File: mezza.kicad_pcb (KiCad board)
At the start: 2 copper layers, 85 x 54 mm, 6 parts, among them P1 CONN_02X20, P2 CONN_02X20

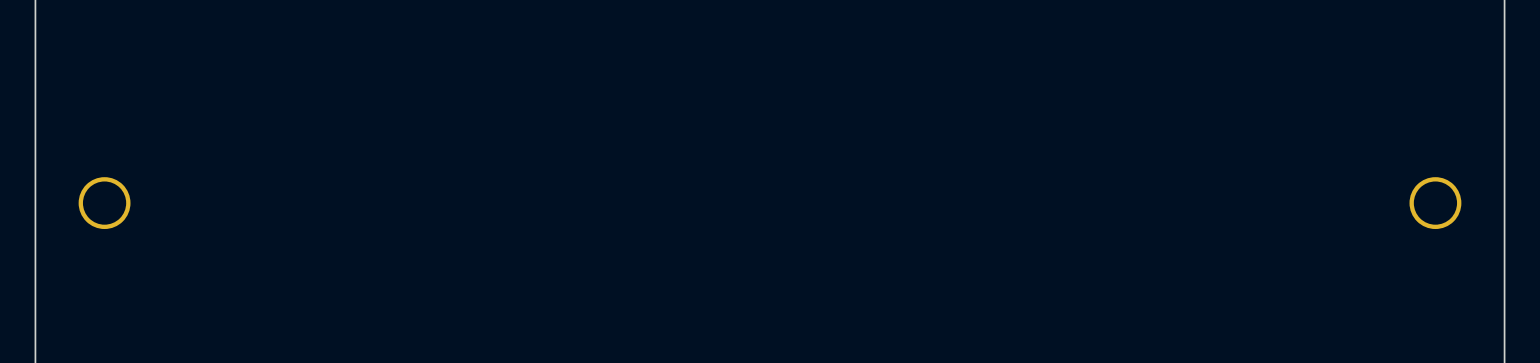
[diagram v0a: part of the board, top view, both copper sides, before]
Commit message: Add dimension markings to layout and correct hole positions
Add dimension markings to the template so that users can see exactly how
things are placed and compare them with the 96Boards spec. At the same
time, fix the position of 2 of the mounting holes and lock all the
footprints so they don't get accidentally changed.

Signed-off-by: Grant Likely <grant.likely@linaro.org>
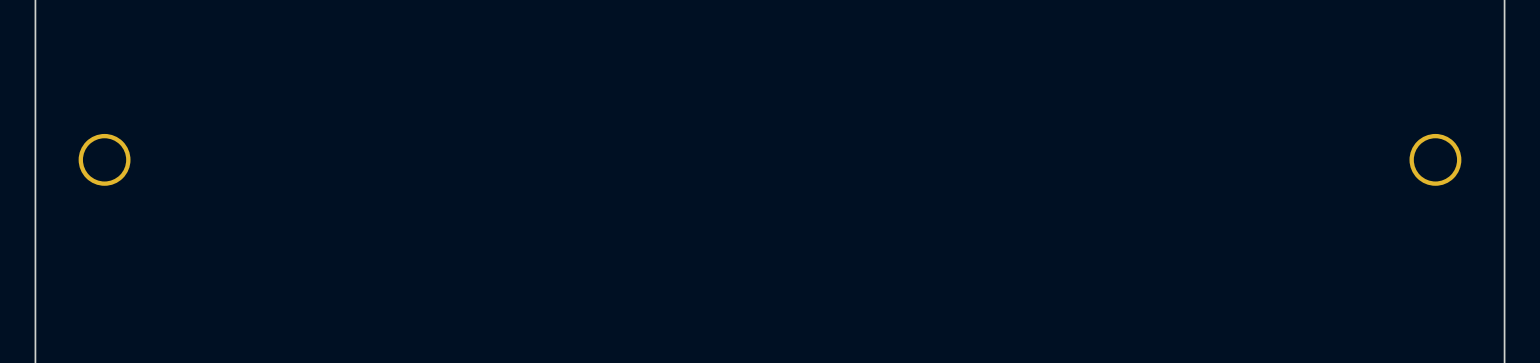
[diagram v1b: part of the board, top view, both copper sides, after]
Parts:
- moved REF** 2.50 mm to (104.0, 135.5)
- moved REF** 2.50 mm to (181.0, 135.5)
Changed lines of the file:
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@@
     (links 44)
     (no_connects 44)
-    (area 99.949999 99.949999 185.049493 154.050001)
+    (area 85.071429 87.15 185.633753 154.050001)
     (thickness 1.6)
-    (drawings 4)
+    (drawings 11)
     (tracks 0)
     (zones 0)
@@
     (47 F.CrtYd user hide)
     (48 B.Fab user hide)
-    (49 F.Fab user hide)
+    (49 F.Fab user)
   )
   (setup
@@
   )
   (module Sensors:Hole_2.5MM locked (layer F.Cu)
-    (at 104 138)
+    (at 104 135.5)
     (fp_text reference REF** (at 0 0.5) (layer F.SilkS) hide
       (effects (font (size 1 1) (thickness 0.15)))
@@
   )
   (module Sensors:Hole_2.5MM locked (layer F.Cu)
-    (at 181 138)
+    (at 181 135.5)
     (fp_text reference REF** (at 0 0.5) (layer F.SilkS) hide
       (effects (font (size 1 1) (thickness 0.15)))
@@
     (pad 1 thru_hole circle (at 0 0) (size 3 3) (drill 2.5) (layers *.Cu *.Mask))
   )
-  (module 96boards:Socket_Strip_SMD_2x20_Pitch2mm (layer F.Cu)
+  (module 96boards:Socket_Strip_SMD_2x20_Pitch2mm locked (layer F.Cu)
     (at 110 105 90)
     (descr "Double row SMD 2mm socket strip, 2x20 contacts")
@@
     )
   )
-  (module 96boards:Pin_Header_SMD_2x20_Pitch2mm (layer B.Cu)
+  (module 96boards:Pin_Header_SMD_2x20_Pitch2mm locked (layer B.Cu)
     (at 110 105 270)
     (descr "Double row SMD 2mm pin header, 2x20 contacts")
@@
     )
   )
+  (dimension 18.5 (width 0.3) (layer F.Fab)
+    (gr_text 18.5mm (at 93.65 144.75 90) (layer F.Fab)
+      (effects (font (size 1.5 1.5) (thickness 0.3)))
+    )
+    (feature1 (pts (xy 104 135.5) (xy 92.3 135.5)))
+    (feature2 (pts (xy 104 154) (xy 92.3 154)))
+    (crossbar (pts (xy 95 154) (xy 95 135.5)))
+    (arrow1a (pts (xy 95 135.5) (xy 95.586421 136.626504)))
+    (arrow1b (pts (xy 95 135.5) (xy 94.413579 136.626504)))
+    (arrow2a (pts (xy 95 154) (xy 95.586421 152.873496)))
+    (arrow2b (pts (xy 95 154) (xy 94.413579 152.873496)))
+  )
+  (dimension 4 (width 0.3) (layer F.Fab)
+    (gr_text 4mm (at 95 107 90) (layer F.Fab)
+      (effects (font (size 1.5 1.5) (thickness 0.3)))
+    )
+    (feature1 (pts (xy 104 100) (xy 92.3 100)))
+    (feature2 (pts (xy 104 104) (xy 92.3 104)))
+    (crossbar (pts (xy 95 104) (xy 95 100)))
+    (arrow1a (pts (xy 95 100) (xy 95.586421 101.126504)))
+    (arrow1b (pts (xy 95 100) (xy 94.413579 101.126504)))
+    (arrow2a (pts (xy 95 104) (xy 95.586421 102.873496)))
+    (arrow2b (pts (xy 95 104) (xy 94.413579 102.873496)))
+  )
+  (dimension 4 (width 0.3) (layer F.Fab)
+    (gr_text 4mm (at 178 95) (layer F.Fab)
+      (effects (font (size 1.5 1.5) (thickness 0.3)))
+    )
+    (feature1 (pts (xy 185 104) (xy 185 92.3)))
+    (feature2 (pts (xy 181 104) (xy 181 92.3)))
+    (crossbar (pts (xy 181 95) (xy 185 95)))
+    (arrow1a (pts (xy 185 95) (xy 183.873496 95.586421)))
+    (arrow1b (pts (xy 185 95) (xy 183.873496 94.413579)))
+    (arrow2a (pts (xy 181 95) (xy 182.126504 95.586421)))
+    (arrow2b (pts (xy 181 95) (xy 182.126504 94.413579)))
+  )
+  (dimension 6 (width 0.3) (layer F.Fab)
+    (gr_text 6mm (at 113 95) (layer F.Fab)
+      (effects (font (size 1.5 1.5) (thickness 0.3)))
+    )
+    (feature1 (pts (xy 110 104) (xy 110 92.3)))
+    (feature2 (pts (xy 104 104) (xy 104 92.3)))
+    (crossbar (pts (xy 104 95) (xy 110 95)))
+    (arrow1a (pts (xy 110 95) (xy 108.873496 95.586421)))
+    (arrow1b (pts (xy 110 95) (xy 108.873496 94.413579)))
+    (arrow2a (pts (xy 104 95) (xy 105.126504 95.586421)))
+    (arrow2b (pts (xy 104 95) (xy 105.126504 94.413579)))
+  )
+  (dimension 4 (width 0.3) (layer F.Fab)
+    (gr_text 4mm (at 97 95) (layer F.Fab)
+      (effects (font (size 1.5 1.5) (thickness 0.3)))
+    )
+    (feature1 (pts (xy 104 104) (xy 104 92.3)))
+    (feature2 (pts (xy 100 104) (xy 100 92.3)))
+    (crossbar (pts (xy 100 95) (xy 104 95)))
+    (arrow1a (pts (xy 104 95) (xy 102.873496 95.586421)))
+    (arrow1b (pts (xy 104 95) (xy 102.873496 94.413579)))
+    (arrow2a (pts (xy 100 95) (xy 101.126504 95.586421)))
+    (arrow2b (pts (xy 100 95) (xy 101.126504 94.413579)))
+  )
+  (dimension 85 (width 0.3) (layer F.Fab)
+    (gr_text 85mm (at 142.5 88.65) (layer F.Fab)
+      (effects (font (size 1.5 1.5) (thickness 0.3)))
+    )
+    (feature1 (pts (xy 185 100) (xy 185 87.3)))
+    (feature2 (pts (xy 100 100) (xy 100 87.3)))
+    (crossbar (pts (xy 100 90) (xy 185 90)))
+    (arrow1a (pts (xy 185 90) (xy 183.873496 90.586421)))
+    (arrow1b (pts (xy 185 90) (xy 183.873496 89.413579)))
+    (arrow2a (pts (xy 100 90) (xy 101.126504 90.586421)))
+    (arrow2b (pts (xy 100 90) (xy 101.126504 89.413579)))
+  )
+  (dimension 54 (width 0.3) (layer F.Fab)
+    (gr_text 54mm (at 88.65 127 90) (layer F.Fab)
+      (effects (font (size 1.5 1.5) (thickness 0.3)))
+    )
+    (feature1 (pts (xy 100 100) (xy 87.3 100)))
+    (feature2 (pts (xy 100 154) (xy 87.3 154)))
+    (crossbar (pts (xy 90 154) (xy 90 100)))
+    (arrow1a (pts (xy 90 100) (xy 90.586421 101.126504)))
+    (arrow1b (pts (xy 90 100) (xy 89.413579 101.126504)))
+    (arrow2a (pts (xy 90 154) (xy 90.586421 152.873496)))
+    (arrow2b (pts (xy 90 154) (xy 89.413579 152.873496)))
+  )
   (gr_line (start 100 154) (end 184.999492 154) (angle 90) (layer Edge.Cuts) (width 0.1))
